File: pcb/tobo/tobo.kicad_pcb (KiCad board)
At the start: 2 copper layers, 57.5 x 61 mm, 92 parts, among them J2 Conn_01x02_Pin, J4 54548-2472, J5 Conn_01x09_Pin, J6 Conn_01x09_Pin, J7 Conn_01x09_Pin, J8 Hroparts Elec TYPE-C-31-M-12, U1 TS5A23167DCUR, U10 5015, U11 5015, U12 5015, U13 5015, U14 CH340E, U15 5015, U16 5015, U18 MAXM20343AMP+, U2 ATmega328P-AN, U3 TS5A23167DCUR, U4 TS5A23167DCUR, U5 TS5A23167DCUR, U6 5015, U7 5015, U8 5015, U9 5015, X1 TestPoint, X2 TestPoint, X7 TestPoint, Y4 TestPoint

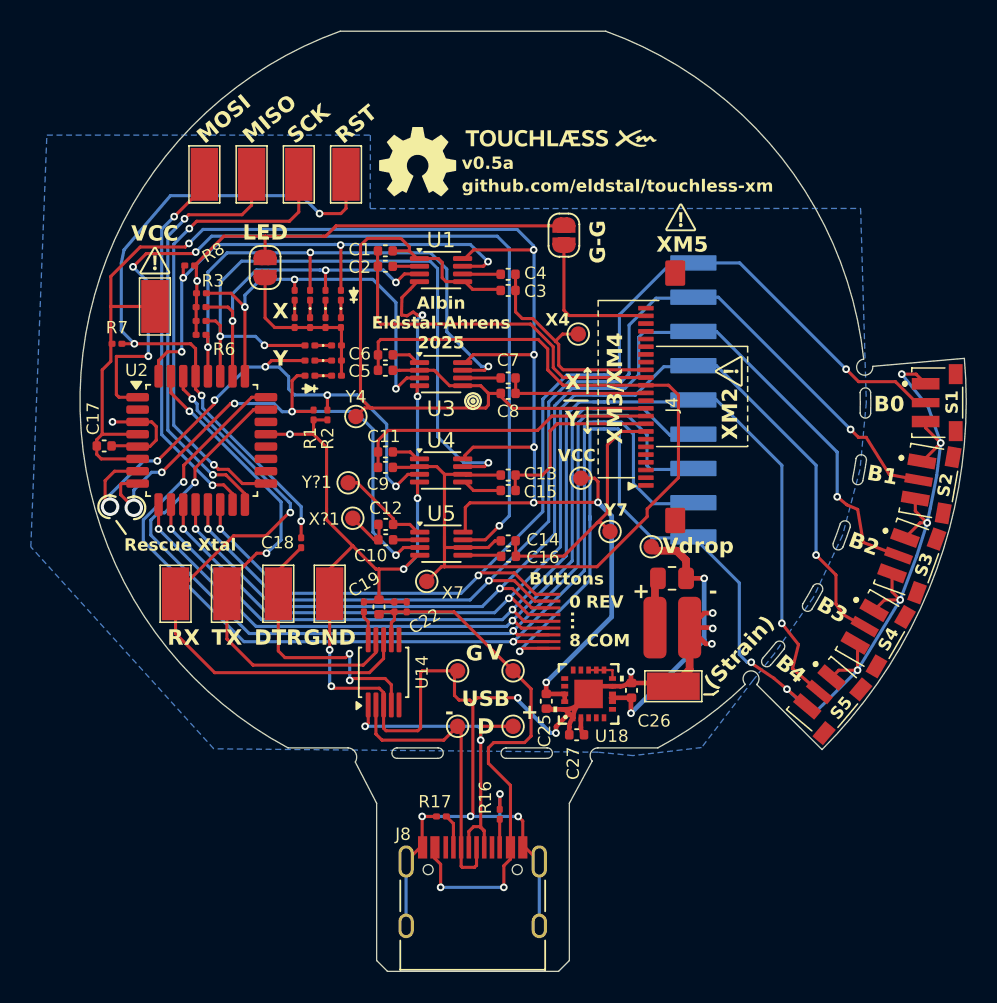
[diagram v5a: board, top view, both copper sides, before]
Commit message: Reworked PCB to use TC7MBL3125CFK bus switches
The old design didn't work, and I suspect it's due to the excessive
capacitance of the analog mux. This chip (~roughly) has been tested
against XM4s on the bench and works great with 1.5pF capacitors.
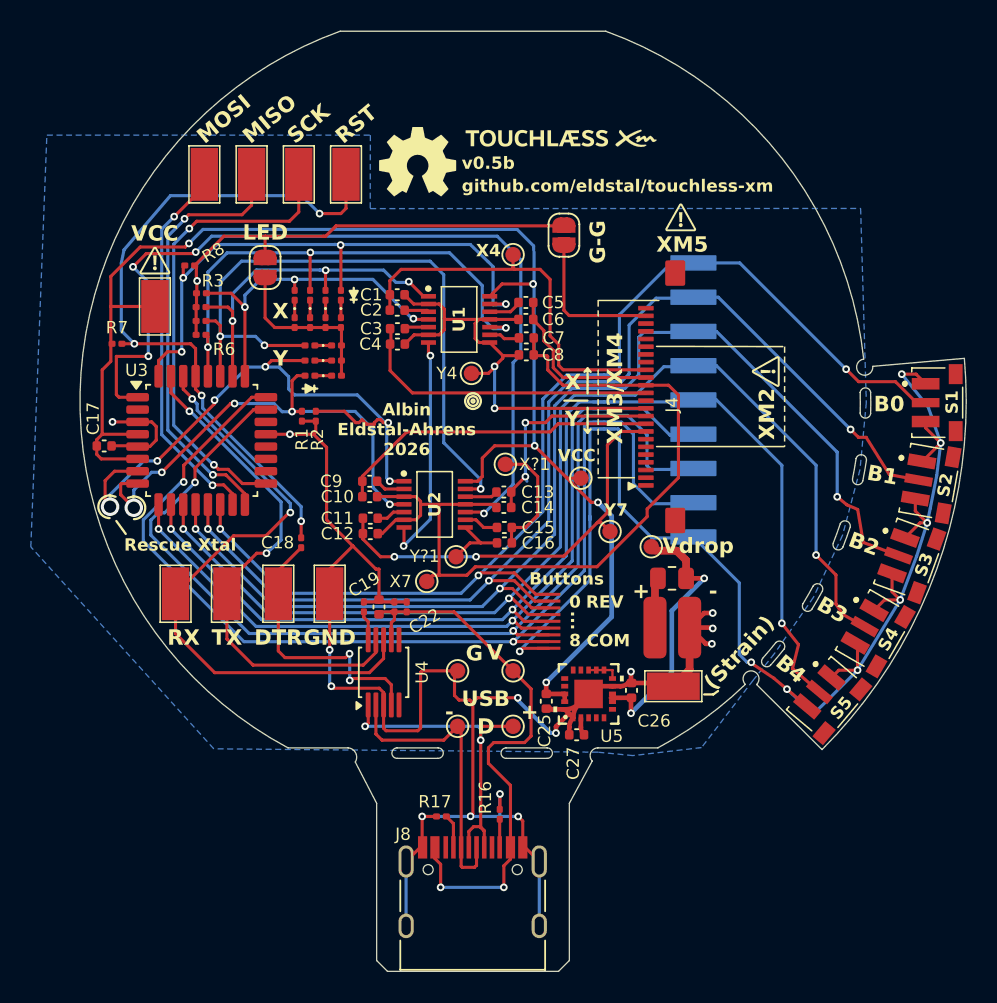
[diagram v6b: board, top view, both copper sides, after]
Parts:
- removed the U3 at (137.9, 88.2)
- removed the U4 at (137.9, 94.5)
- removed the U5 at (137.9, 99.2)
- added U2: ~, tobo-footprints:VSSOP50P400X100-14N, F.Cu at (137.5, 96.7)
- U1: value TS5A23167DCUR -> ~; footprint tobo-footprints:VSSOP-8_2.3x2mm_P0.5mm_narrowpads -> tobo-footprints:VSSOP50P400X100-14N
- moved X?1 10.5 mm to (142.1, 94.1)
- moved Y?1 8.49 mm to (138.9, 100.1)
- moved Y4 8.01 mm to (139.9, 88.2)
- moved X1 6.66 mm to (142.6, 80.5)
- moved U1 3.41 mm to (139.1, 84.7)
- moved C1 2.95 mm to (135.1, 83.1)
- moved C2 2.95 mm to (135.1, 84.1)
- moved C7 2.86 mm to (143.5, 85.9)
- moved C8 2.76 mm to (143.5, 87.0)
- moved C6 2.21 mm to (143.4, 84.7)
- moved C5 2.16 mm to (143.4, 83.6)
- moved C10 2.16 mm to (133.3, 96.2)
- moved C9 2.16 mm to (133.3, 95.2)
- moved C3 1.87 mm to (135.1, 85.3)
- moved C4 1.87 mm to (135.1, 86.3)
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- renumbered C9 to C10, C12 to C11, C10 to C12, C15 to C14, C14 to C15, C6 to C3, C5 to C4, C4 to C5, C3 to C6, C11 to C9, U2 to U3, U14 to U4, U18 to U5
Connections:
- C1 pad 2: /X3 -> /X4
- C10 pad 1: /Y5 -> /Y6
- C11 pad 1: Net-(U5-NC1) -> Net-(U2-A2)
- C11 pad 2: Net-(C10-Pad1) -> /Y7
- C12 pad 1: Net-(C10-Pad1) -> /Y7
- C12 pad 2: Net-(U5-COM1) -> /X2
- C13 pad 1: /X2 -> Net-(U2-A4)
- C13 pad 2: /Y6 -> /Y5
- C14 pad 1: /Y6 -> /Y5
- C14 pad 2: Net-(U4-NC2) -> /X2
- C15 pad 1: /X2 -> Net-(U2-A3)
- C15 pad 2: /Y7 -> Net-(C15-Pad2)
- C16 pad 1: /Y7 -> Net-(C15-Pad2)
- C16 pad 2: Net-(U5-NC2) -> Net-(U2-B3)
- C2 pad 1: /X3 -> /X4
- C2 pad 2: Net-(U1-COM1) -> Net-(U1-B1)
- C3 pad 1: Net-(U3-NC1) -> Net-(U1-A2)
- C3 pad 2: /X2 -> /X1
- C4 pad 1: /X2 -> /X1
- C5 pad 1: Net-(U1-COM2) -> Net-(U1-A4)
- C5 pad 2: /X4 -> /X3
- C6 pad 1: /X4 -> /X3
- C7 pad 1: Net-(U3-COM2) -> Net-(U1-A3)
- C7 pad 2: /X1 -> /X2
- C8 pad 1: /X1 -> /X2
- C9 pad 2: /Y5 -> /Y6
- U1 pad 1: /Y4 -> /4,4
- U1 pad 2: Net-(U1-COM1) -> /Y4
- U1 pad 3: /4,4 -> Net-(U1-B1)
- U1 pad 4: GND -> /1,4
- U1 pad 5: /Y4 -> Net-(U1-A2)
- U1 pad 6: Net-(U1-COM2) -> /Y4
- U1 pad 7: /3,4 -> GND
- U1 pad 8: VCC -> /Y4
- X?1 pad 1: Net-(C10-Pad1) -> Net-(C15-Pad2)
- Y?1 pad 1: Net-(U5-NC1) -> Net-(U2-B3)
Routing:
- net /Y4: track 51.6 -> 32.5 mm, vias 0 -> 2
- net VCC: track 108.7 -> 93.6 mm, vias 7 -> 5
- net /X2: track 66.7 -> 53.2 mm
- net /X3: track 24.4 -> 11.0 mm
- net /Y7: track 16.4 -> 27.2 mm, vias 0 -> 2
- net GND: track 262.3 -> 251.7 mm, vias 27 -> 25
- net /X1: track 9.54 -> 20.0 mm
- net /X4: track 15.2 -> 25.5 mm
- net /Y6: track 12.3 -> 21.1 mm
- net Net-(C15-Pad2): track 0.00 -> 7.93 mm
- net /Y5: track 19.8 -> 13.8 mm, vias 0 -> 2
- net Net-(U5-NC1): track 6.04 -> 0.00 mm
- net /2,7: track 37.4 -> 32.5 mm
- net /1,4: track 26.9 -> 22.2 mm
- net Net-(U2-B3): track 0.00 -> 4.45 mm
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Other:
- board text added: "Albin Eldstal-Ahrens 2026"
- board text added: "v0.5b"
- board text removed: "Albin Eldstal-Ahrens 2025"
- board text removed: "v0.5a"

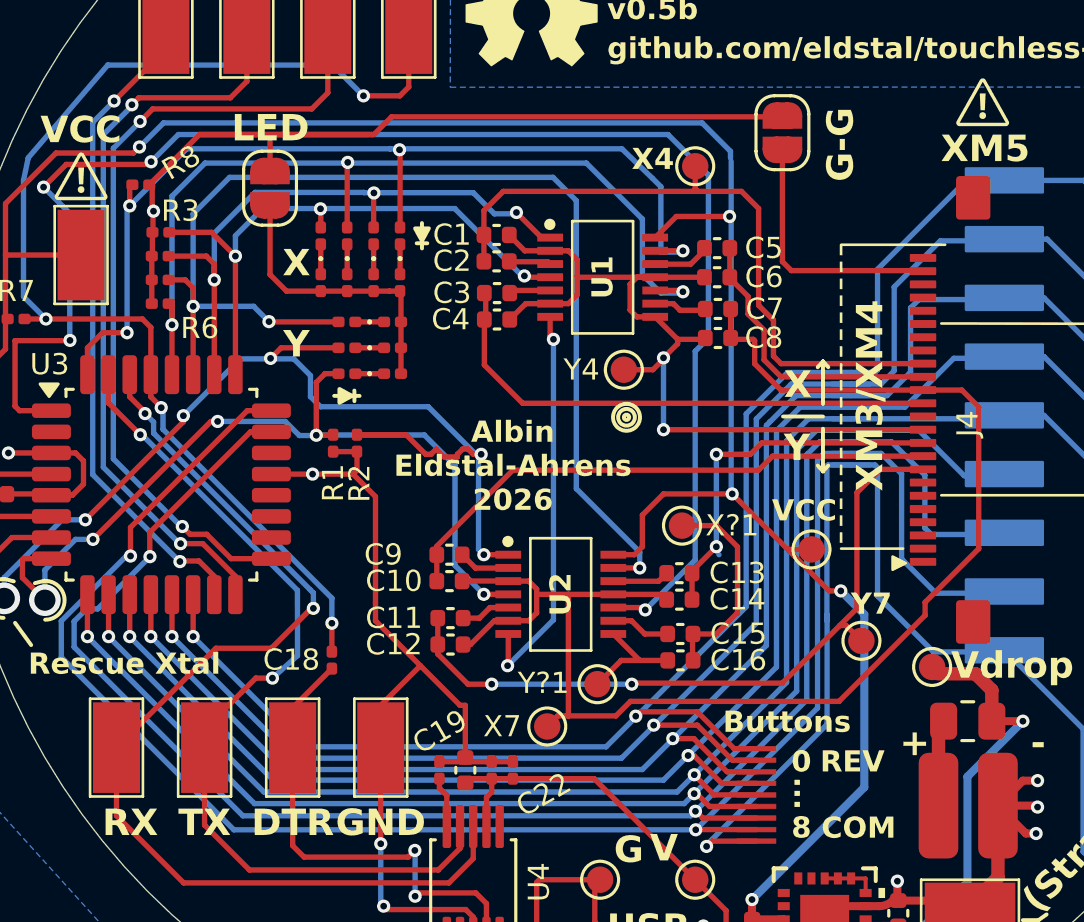
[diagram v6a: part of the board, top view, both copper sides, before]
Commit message: Unused controller now has through-hole caps for experimentation
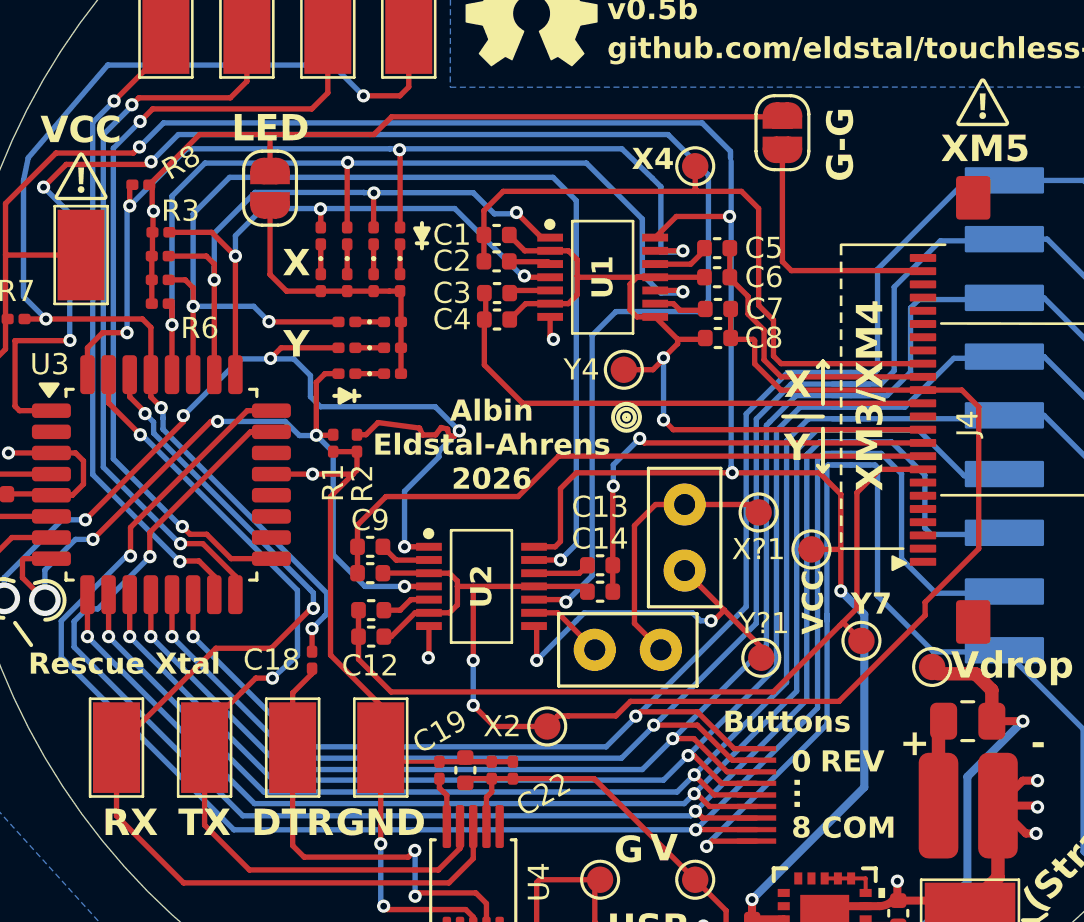
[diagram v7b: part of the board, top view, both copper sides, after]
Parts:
- C15, C16: footprint Capacitor_SMD:C_0402_1005Metric -> Capacitor_THT:C_Disc_D5.0mm_W2.5mm_P2.50mm
- moved Y?1 6.28 mm to (145.1, 99.1)
- moved C16 5.90 mm to (142.2, 93.3), turned to -90 degrees
- moved C15 3.29 mm to (138.8, 98.8)
- moved C13 3.01 mm to (139.0, 95.6)
- moved C14 3.01 mm to (139.0, 96.6)
- moved C10 3.01 mm to (130.3, 95.9)
- moved C11 3.01 mm to (130.3, 97.3)
- moved C12 3.01 mm to (130.3, 98.3)
- moved C9 3.01 mm to (130.3, 94.9)
- moved U2 3.01 mm to (134.5, 96.4)
- moved X?1 2.94 mm to (145.0, 93.6)
- moved C18 0.75 mm to (128.1, 99.2)
- renumbered X7 to X2
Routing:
- net GND: track 251.7 -> 236.2 mm
- net Net-(U2-B3): track 4.45 -> 14.0 mm, vias 0 -> 2
- net VCC: track 93.6 -> 99.1 mm
- net /Y7: track 27.2 -> 30.8 mm, vias 2 -> 0
- net /Y5: track 13.8 -> 17.0 mm
- net /Y6: track 21.1 -> 24.3 mm
- net /2,7: track 32.5 -> 29.5 mm
- net /X2: track 53.2 -> 56.2 mm, vias 0 -> 2
- net /?,?: track 57.5 -> 60.2 mm
- net Net-(C15-Pad2): track 7.93 -> 10.3 mm
- net /DTR: track 19.8 -> 18.0 mm
- net /2,5: track 44.8 -> 43.8 mm
- net Net-(U2-A3): track 2.26 -> 2.88 mm

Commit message: PCB tweaks and prettification
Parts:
- C15, C16: footprint Capacitor_THT:C_Disc_D5.0mm_W2.5mm_P2.50mm -> tobo-footprints:C_Disc_D5.0mm_W2.5mm_P2.50mm
- moved X1 7.12 mm to (147.0, 86.1)
- renumbered X2 to X7
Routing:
- net /X4: track 25.5 -> 26.0 mm
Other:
- board text added: "C"
- board text added: "Cut HERE"
- board text added: "For rescue Xtal"
- board text added: "v0.5c"
- board text removed: "v0.5b"
